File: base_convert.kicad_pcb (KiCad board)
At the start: 2 copper layers, 72 x 106 mm, 53 parts, among them SW1 SW_Push, SW10 SW_Push, SW11 SW_Push, SW12 SW_Push, SW13 SW_Push, SW14 SW_Push, SW15 SW_Push, SW16 SW_Push, SW17 SW_Push, SW18 SW_Push, SW19 SW_Push, SW2 SW_Push, SW20 SW_Push, SW21 SW_Push, SW22 SW_Push, SW23 SW_Push, SW24 SW_Push, SW25 SW_Push, SW26 SW_Push, SW27 SW_Push, SW28 SW_Push, SW29 SW_Push, SW3 SW_Push, SW30 SW_Push, SW31 SW_Push, SW32 SW_Push, SW4 SW_Push, SW5 SW_Push, SW6 SW_Push, SW7 SW_Push, SW8 SW_Push, SW9 SW_Push

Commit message: perlimanary prototype render
perlimanary prototype render complete
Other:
- board text added: "0"
- board text added: "1"
- board text added: "10"
- board text added: "11"
- board text added: "12"
- board text added: "13"
- board text added: "14"
- board text added: "15"
- board text added: "2"
- board text added: "3"
- board text added: "4"
- board text added: "5"
- board text added: "6"
- board text added: "7"
- board text added: "8"
- board text added: "9"
- board text added: "A"
- board text added: "B"
- board text added: "C"
- board text added: "D"
- board text added: "DEC"
- board text added: "E"
- board text added: "F"
- board text added: "HEX"

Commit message: update 7-segment display part number
Due to mismatch of display face using a mix of 4 digit and 1 digit displays does not look good. Swtiching all displays to be made up of 2 digit 7-segment display. Decimal display will have extra unused digit.
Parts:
- removed AFF1, AFF2, AFF3, AFF4, AFF5: DA04-11, Displays_7-Segment:DA04-11SURKWA
- added BT1: Battery, MPD:BC2AAPC, F.Cu at (195.2, 124.5)
- added C1: 10uF, Capacitors_SMD:C_0805, F.Cu at (335.6, 51.4)
- added C2: 100nF, Capacitors_SMD:C_0805, F.Cu at (340.1, 51.4)
- added DS1: LTD-4608JR, Lite-On:Display_Lite-On_LTD-4608JR, F.Cu at (189.6, 64.1)
- added DS2: LTD-4608JR, Lite-On:Display_Lite-On_LTD-4608JR, F.Cu at (96.0, 64.1)
- added DS3: LTD-4608JR, Lite-On:Display_Lite-On_LTD-4608JR, F.Cu at (121.3, 64.1)
- added DS4: LTD-4608JR, Lite-On:Display_Lite-On_LTD-4608JR, F.Cu at (176.8, 37.7)
- added DS5: LTD-4608JR, Lite-On:Display_Lite-On_LTD-4608JR, F.Cu at (152.8, 33.9)
- added J1: ISP, Pin_Headers:Pin_Header_Straight_1x04_Pitch2.54mm, F.Cu at (379.8, 21.2)
- added Q1: Q_PMOS_GSD, TO_SOT_Packages_SMD:SOT-23, F.Cu at (325.0, 52.4)
- added Q10: Q_PNP_BEC, TO_SOT_Packages_SMD:SOT-23, F.Cu at (269.3, 94.6)
- added Q11: Q_NPN_BEC, TO_SOT_Packages_SMD:SOT-23, F.Cu at (251.5, 100.0)
- added Q12: Q_NPN_BEC, TO_SOT_Packages_SMD:SOT-23, F.Cu at (252.7, 123.5)
- added Q13: Q_NPN_BEC, TO_SOT_Packages_SMD:SOT-23, F.Cu at (242.5, 107.1)
- added Q14: Q_NPN_BEC, TO_SOT_Packages_SMD:SOT-23, F.Cu at (224.6, 107.1)
- added Q15: Q_NPN_BEC, TO_SOT_Packages_SMD:SOT-23, F.Cu at (233.5, 107.1)
- added Q16: Q_NPN_BEC, TO_SOT_Packages_SMD:SOT-23, F.Cu at (217.4, 79.4)
- added Q17: Q_NPN_BEC, TO_SOT_Packages_SMD:SOT-23, F.Cu at (242.5, 100.0)
- added Q18: Q_PNP_BEC, TO_SOT_Packages_SMD:SOT-23, F.Cu at (353.3, 79.9)
- added Q19: Q_PNP_BEC, TO_SOT_Packages_SMD:SOT-23, F.Cu at (333.3, 96.8)
- added Q2: Q_PNP_BEC, TO_SOT_Packages_SMD:SOT-23, B.Cu at (181.7, 64.3)
- added Q20: Q_PNP_BEC, TO_SOT_Packages_SMD:SOT-23, F.Cu at (349.4, 86.9)
- added Q21: Q_PNP_BEC, TO_SOT_Packages_SMD:SOT-23, F.Cu at (340.5, 89.7)
- added Q22: Q_NPN_BEC, TO_SOT_Packages_SMD:SOT-23, F.Cu at (344.3, 72.8)
- added Q23: Q_NPN_BEC, TO_SOT_Packages_SMD:SOT-23, F.Cu at (344.3, 79.9)
- added Q24: Q_NPN_BEC, TO_SOT_Packages_SMD:SOT-23, F.Cu at (353.3, 72.8)
- added Q25: Q_NPN_BEC, TO_SOT_Packages_SMD:SOT-23, F.Cu at (324.4, 96.6)
- added Q26: Q_PNP_BEC, TO_SOT_Packages_SMD:SOT-23, F.Cu at (313.9, 20.7)
- added Q27: Q_NPN_BEC, TO_SOT_Packages_SMD:SOT-23, F.Cu at (313.9, 20.7)
- added Q3: Q_PNP_BEC, TO_SOT_Packages_SMD:SOT-23, F.Cu at (251.4, 107.1)
- added Q4: Q_PNP_BEC, TO_SOT_Packages_SMD:SOT-23, B.Cu at (234.4, 58.7)
- added Q5: Q_PNP_BEC, TO_SOT_Packages_SMD:SOT-23, B.Cu at (227.4, 60.2)
- added Q6: Q_PNP_BEC, TO_SOT_Packages_SMD:SOT-23, F.Cu at (237.3, 126.2)
- added Q7: Q_PNP_BEC, TO_SOT_Packages_SMD:SOT-23, F.Cu at (274.4, 87.5)
- added Q8: Q_PNP_BEC, TO_SOT_Packages_SMD:SOT-23, F.Cu at (257.7, 60.5)
- added Q9: Q_PNP_BEC, TO_SOT_Packages_SMD:SOT-23, F.Cu at (260.4, 107.1)
- added R1: 20k, Resistors_SMD:R_0805, F.Cu at (331.8, 51.6)
- added R10: 4.7k, Resistors_SMD:R_0805, F.Cu at (287.9, 84.5)
- added R11: 4.7k, Resistors_SMD:R_0805, F.Cu at (284.3, 86.1)
- added R12: 1k, Resistors_SMD:R_0603, B.Cu at (277.3, 99.0)
- added R13: 1k, Resistors_SMD:R_0603, B.Cu at (270.1, 106.0)
- added R14: 1k, Resistors_SMD:R_0603, B.Cu at (280.6, 96.8)
- added R15: 1k, Resistors_SMD:R_0603, B.Cu at (273.4, 106.0)
- added R16: 1k, Resistors_SMD:R_0603, B.Cu at (233.1, 73.4)
- added R17: 1k, Resistors_SMD:R_0603, B.Cu at (218.7, 71.7)
- added R18: 1k, Resistors_SMD:R_0603, B.Cu at (240.1, 72.4)
- added R19: 4.7k, Resistors_SMD:R_0805, F.Cu at (287.9, 89.9)
- added R2: 20k, Resistors_SMD:R_0805, F.Cu at (331.8, 57.1)
- added R20: 4.7k, Resistors_SMD:R_0805, F.Cu at (262.9, 93.7)
- added R21: 4.7k, Resistors_SMD:R_0805, F.Cu at (290.3, 79.0)
- added R22: 4.7k, Resistors_SMD:R_0805, F.Cu at (291.5, 84.5)
- added R23: 4.7k, Resistors_SMD:R_0805, F.Cu at (266.7, 100.8)
- added R24: 4.7k, Resistors_SMD:R_0805, F.Cu at (280.7, 86.1)
- added R25: 4.7k, Resistors_SMD:R_0805, F.Cu at (286.7, 79.0)
- added R26: 4.7k, Resistors_SMD:R_0805, F.Cu at (359.5, 84.5)
- added R27: 4.7k, Resistors_SMD:R_0805, F.Cu at (339.6, 101.4)
- added R28: 4.7k, Resistors_SMD:R_0805, F.Cu at (355.7, 86.1)
- added R29: 4.7k, Resistors_SMD:R_0805, F.Cu at (350.3, 93.1)
- added R3: 4.7k, Resistors_SMD:R_0805, B.Cu at (236.9, 64.2)
- added R30: 1k, Resistors_SMD:R_0603, F.Cu at (346.3, 98.4)
- added R31: 1k, Resistors_SMD:R_0603, F.Cu at (343.0, 95.7)
- added R32: 1k, Resistors_SMD:R_0603, F.Cu at (304.2, 101.7)
- added R33: 1k, Resistors_SMD:R_0603, F.Cu at (300.9, 101.7)
- added R34: 4.7k, Resistors_SMD:R_0805, F.Cu at (359.5, 79.0)
- added R35: 4.7k, Resistors_SMD:R_0805, F.Cu at (339.6, 95.9)
- added R36: 4.7k, Resistors_SMD:R_0805, F.Cu at (359.6, 72.0)
- added R37: 4.7k, Resistors_SMD:R_0805, F.Cu at (346.7, 93.1)
- added R38, R40: 4.7k, Resistors_SMD:R_0805, F.Cu at (313.9, 20.7)
- added R39: 1k, Resistors_SMD:R_0603, F.Cu at (313.9, 20.7)
- added R4: 4.7k, Resistors_SMD:R_0805, F.Cu at (266.6, 106.2)
- added R5: 4.7k, Resistors_SMD:R_0805, F.Cu at (270.3, 100.8)
- added R6: 4.7k, Resistors_SMD:R_0805, F.Cu at (280.7, 91.5)
- added R7: 4.7k, Resistors_SMD:R_0805, F.Cu at (284.3, 91.5)
- added R8: 4.7k, Resistors_SMD:R_0805, F.Cu at (273.9, 100.8)
- added R9: 4.7k, Resistors_SMD:R_0805, F.Cu at (293.9, 79.0)
- added SW33: B, Buttons_Switches_THT:SW_PUSH_6mm, F.Cu at (125.0, 137.5)
- added SW34: F, Buttons_Switches_THT:SW_PUSH_6mm, F.Cu at (125.0, 97.5)
- added U1: MSP430FR4133IPMR, Housings_QFP:LQFP-64_10x10mm_Pitch0.5mm, F.Cu at (102.5, 124.6)
- D1: value LED -> BIT3; footprint LEDs:LED_D3.0mm -> LEDs:LED_D5.0mm
- D10: value LED -> BIT5; footprint LEDs:LED_D3.0mm -> LEDs:LED_D5.0mm
- D11: value LED -> BIT9; footprint LEDs:LED_D3.0mm -> LEDs:LED_D5.0mm
- D12: value LED -> BIT13; footprint LEDs:LED_D3.0mm -> LEDs:LED_D5.0mm
- D13: value LED -> BIT0; footprint LEDs:LED_D3.0mm -> LEDs:LED_D5.0mm
- D14: value LED -> BIT4; footprint LEDs:LED_D3.0mm -> LEDs:LED_D5.0mm
- D15: value LED -> BIT8; footprint LEDs:LED_D3.0mm -> LEDs:LED_D5.0mm
- D16: value LED -> BIT12; footprint LEDs:LED_D3.0mm -> LEDs:LED_D5.0mm
- D2: value LED -> BIT7; footprint LEDs:LED_D3.0mm -> LEDs:LED_D5.0mm
- D3: value LED -> BIT11; footprint LEDs:LED_D3.0mm -> LEDs:LED_D5.0mm
- D4: value LED -> BIT15; footprint LEDs:LED_D3.0mm -> LEDs:LED_D5.0mm
- D5: value LED -> BIT2; footprint LEDs:LED_D3.0mm -> LEDs:LED_D5.0mm
- D6: value LED -> BIT6; footprint LEDs:LED_D3.0mm -> LEDs:LED_D5.0mm
- D7: value LED -> BIT10; footprint LEDs:LED_D3.0mm -> LEDs:LED_D5.0mm
- D8: value LED -> BIT14; footprint LEDs:LED_D3.0mm -> LEDs:LED_D5.0mm
- D9: value LED -> BIT1; footprint LEDs:LED_D3.0mm -> LEDs:LED_D5.0mm
- SW1: value SW_Push -> CLEAR; footprint Buttons_Switches_SMD:SW_SPST_FSMSM -> Buttons_Switches_THT:SW_PUSH_6mm
- SW10: value SW_Push -> B13; footprint Buttons_Switches_SMD:SW_SPST_FSMSM -> Buttons_Switches_THT:SW_PUSH_6mm
- SW11: value SW_Push -> B2; footprint Buttons_Switches_SMD:SW_SPST_FSMSM -> Buttons_Switches_THT:SW_PUSH_6mm
- SW12: value SW_Push -> B6; footprint Buttons_Switches_SMD:SW_SPST_FSMSM -> Buttons_Switches_THT:SW_PUSH_6mm
- SW13: value SW_Push -> B10; footprint Buttons_Switches_SMD:SW_SPST_FSMSM -> Buttons_Switches_THT:SW_PUSH_6mm
- SW14: value SW_Push -> B14; footprint Buttons_Switches_SMD:SW_SPST_FSMSM -> Buttons_Switches_THT:SW_PUSH_6mm
- SW15: value SW_Push -> B3; footprint Buttons_Switches_SMD:SW_SPST_FSMSM -> Buttons_Switches_THT:SW_PUSH_6mm
- SW16: value SW_Push -> B7; footprint Buttons_Switches_SMD:SW_SPST_FSMSM -> Buttons_Switches_THT:SW_PUSH_6mm
- SW17: value SW_Push -> B11; footprint Buttons_Switches_SMD:SW_SPST_FSMSM -> Buttons_Switches_THT:SW_PUSH_6mm
- SW18: value SW_Push -> B15; footprint Buttons_Switches_SMD:SW_SPST_FSMSM -> Buttons_Switches_THT:SW_PUSH_6mm
- SW19: value SW_Push -> 0; footprint Buttons_Switches_SMD:SW_SPST_FSMSM -> Buttons_Switches_THT:SW_PUSH_6mm
- SW2: value SW_Push -> SELECT; footprint Buttons_Switches_SMD:SW_SPST_FSMSM -> Switch_CK:DP4T_SS-24E06-TG5P
- SW20: value SW_Push -> 4; footprint Buttons_Switches_SMD:SW_SPST_FSMSM -> Buttons_Switches_THT:SW_PUSH_6mm
- SW21: value SW_Push -> 8; footprint Buttons_Switches_SMD:SW_SPST_FSMSM -> Buttons_Switches_THT:SW_PUSH_6mm
- SW22: value SW_Push -> C; footprint Buttons_Switches_SMD:SW_SPST_FSMSM -> Buttons_Switches_THT:SW_PUSH_6mm
- SW23: value SW_Push -> 1; footprint Buttons_Switches_SMD:SW_SPST_FSMSM -> Buttons_Switches_THT:SW_PUSH_6mm
- SW24: value SW_Push -> 5; footprint Buttons_Switches_SMD:SW_SPST_FSMSM -> Buttons_Switches_THT:SW_PUSH_6mm
- SW25: value SW_Push -> 9; footprint Buttons_Switches_SMD:SW_SPST_FSMSM -> Buttons_Switches_THT:SW_PUSH_6mm
- SW26: value SW_Push -> D; footprint Buttons_Switches_SMD:SW_SPST_FSMSM -> Buttons_Switches_THT:SW_PUSH_6mm
- SW27: value SW_Push -> 2; footprint Buttons_Switches_SMD:SW_SPST_FSMSM -> Buttons_Switches_THT:SW_PUSH_6mm
- SW28: value SW_Push -> 6; footprint Buttons_Switches_SMD:SW_SPST_FSMSM -> Buttons_Switches_THT:SW_PUSH_6mm
- SW29: value SW_Push -> A; footprint Buttons_Switches_SMD:SW_SPST_FSMSM -> Buttons_Switches_THT:SW_PUSH_6mm
- SW3: value SW_Push -> B0; footprint Buttons_Switches_SMD:SW_SPST_FSMSM -> Buttons_Switches_THT:SW_PUSH_6mm
- SW30: value SW_Push -> E; footprint Buttons_Switches_SMD:SW_SPST_FSMSM -> Buttons_Switches_THT:SW_PUSH_6mm
- SW31: value SW_Push -> 3; footprint Buttons_Switches_SMD:SW_SPST_FSMSM -> Buttons_Switches_THT:SW_PUSH_6mm
- SW32: value SW_Push -> 7; footprint Buttons_Switches_SMD:SW_SPST_FSMSM -> Buttons_Switches_THT:SW_PUSH_6mm
- SW4: value SW_Push -> B4; footprint Buttons_Switches_SMD:SW_SPST_FSMSM -> Buttons_Switches_THT:SW_PUSH_6mm
- SW5: value SW_Push -> B8; footprint Buttons_Switches_SMD:SW_SPST_FSMSM -> Buttons_Switches_THT:SW_PUSH_6mm
- SW6: value SW_Push -> B12; footprint Buttons_Switches_SMD:SW_SPST_FSMSM -> Buttons_Switches_THT:SW_PUSH_6mm
- SW7: value SW_Push -> B1; footprint Buttons_Switches_SMD:SW_SPST_FSMSM -> Buttons_Switches_THT:SW_PUSH_6mm
- SW8: value SW_Push -> B5; footprint Buttons_Switches_SMD:SW_SPST_FSMSM -> Buttons_Switches_THT:SW_PUSH_6mm
- SW9: value SW_Push -> B9; footprint Buttons_Switches_SMD:SW_SPST_FSMSM -> Buttons_Switches_THT:SW_PUSH_6mm
- moved D4 111.7 mm to (92.9, 78.9), turned to 0 degrees
- moved SW29 96.1 mm to (125.0, 147.5)
- moved SW1 92.1 mm to (167.0, 147.5), turned to 0 degrees
- moved D8 88.0 mm to (100.4, 78.9), turned to 0 degrees
- moved D3 86.6 mm to (122.9, 78.9), turned to 0 degrees
- moved SW30 83.0 mm to (125.0, 107.5)
- moved SW6 83.0 mm to (114.4, 91.7)
- moved SW18 79.9 mm to (91.9, 91.7), turned to 90 degrees
- moved SW27 76.0 mm to (153.0, 137.5)
- moved SW26 75.0 mm to (125.0, 117.5)
- moved SW10 74.1 mm to (106.9, 91.7)
- moved SW32 69.0 mm to (139.0, 117.5)
- moved SW23 68.4 mm to (139.0, 137.5)
- moved SW14 65.3 mm to (99.4, 91.7)
- moved D12 64.7 mm to (107.9, 78.9), turned to 0 degrees
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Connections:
- D1 pad 1: Net-(D1-Pad1) -> /Binary Display/BIT3
- D10 pad 1: Net-(D10-Pad1) -> /Binary Display/BIT1
- D11 pad 1: Net-(D11-Pad1) -> /Binary Display/BIT1
- D12 pad 1: Net-(D12-Pad1) -> /Binary Display/BIT1
- D13 pad 1: Net-(D13-Pad1) -> /Binary Display/BIT0
- D13 pad 2: Net-(D13-Pad2) -> Net-(D1-Pad2)
- D14 pad 1: Net-(D14-Pad1) -> /Binary Display/BIT0
- D14 pad 2: Net-(D14-Pad2) -> Net-(D10-Pad2)
- D15 pad 1: Net-(D15-Pad1) -> /Binary Display/BIT0
- D15 pad 2: Net-(D15-Pad2) -> Net-(D11-Pad2)
- D16 pad 1: Net-(D16-Pad1) -> /Binary Display/BIT0
- D16 pad 2: Net-(D16-Pad2) -> Net-(D12-Pad2)
- D2 pad 1: Net-(D2-Pad1) -> /Binary Display/BIT3
- D2 pad 2: Net-(D2-Pad2) -> Net-(D10-Pad2)
- D3 pad 1: Net-(D3-Pad1) -> /Binary Display/BIT3
- D3 pad 2: Net-(D3-Pad2) -> Net-(D11-Pad2)
- D4 pad 1: Net-(D4-Pad1) -> /Binary Display/BIT3
- D4 pad 2: Net-(D4-Pad2) -> Net-(D12-Pad2)
- D5 pad 1: Net-(D5-Pad1) -> /Binary Display/BIT2
- D5 pad 2: Net-(D5-Pad2) -> Net-(D1-Pad2)
- D6 pad 1: Net-(D6-Pad1) -> /Binary Display/BIT2
- D6 pad 2: Net-(D6-Pad2) -> Net-(D10-Pad2)
- D7 pad 1: Net-(D7-Pad1) -> /Binary Display/BIT2
- D7 pad 2: Net-(D7-Pad2) -> Net-(D11-Pad2)
- D8 pad 1: Net-(D8-Pad1) -> /Binary Display/BIT2
- D8 pad 2: Net-(D8-Pad2) -> Net-(D12-Pad2)
- D9 pad 1: Net-(D9-Pad1) -> /Binary Display/BIT1
- D9 pad 2: Net-(D9-Pad2) -> Net-(D1-Pad2)
- SW1 pad 1: Net-(SW1-Pad1) -> GND
- SW1 pad 2: Net-(SW1-Pad2) -> /CLEAR
- SW10 pad 1: Net-(SW10-Pad1) -> /BCOL1
- SW10 pad 2: Net-(SW10-Pad2) -> /BROW3
- SW11 pad 1: Net-(SW11-Pad1) -> /BCOL2
- SW11 pad 2: Net-(SW11-Pad2) -> /BROW0
- SW12 pad 1: Net-(SW12-Pad1) -> /BCOL2
- SW12 pad 2: Net-(SW12-Pad2) -> /BROW1
- SW13 pad 1: Net-(SW13-Pad1) -> /BCOL2
- SW13 pad 2: Net-(SW13-Pad2) -> /BROW2
- SW14 pad 1: Net-(SW14-Pad1) -> /BCOL2
- SW14 pad 2: Net-(SW14-Pad2) -> /BROW3
- SW15 pad 1: Net-(SW15-Pad1) -> /BCOL3
- SW15 pad 2: Net-(SW15-Pad2) -> /BROW0
- SW16 pad 1: Net-(SW16-Pad1) -> /BCOL3
- SW16 pad 2: Net-(SW16-Pad2) -> /BROW1
- SW17 pad 1: Net-(SW17-Pad1) -> /BCOL3
- SW17 pad 2: Net-(SW17-Pad2) -> /BROW2
- SW18 pad 1: Net-(SW18-Pad1) -> /BCOL3
- SW18 pad 2: Net-(SW18-Pad2) -> /BROW3
- SW19 pad 1: Net-(SW19-Pad1) -> /COL0
- SW19 pad 2: Net-(SW19-Pad2) -> /ROW0
- SW2 pad 1: Net-(SW2-Pad1) -> (no net)
- SW2 pad 2: Net-(SW2-Pad2) -> /DEC_INPUT
- SW20 pad 1: Net-(SW20-Pad1) -> /COL0
- SW20 pad 2: Net-(SW20-Pad2) -> /ROW1
- SW21 pad 1: Net-(SW21-Pad1) -> /COL0
- SW21 pad 2: Net-(SW21-Pad2) -> /ROW2
- SW22 pad 1: Net-(SW22-Pad1) -> /COL0
- SW22 pad 2: Net-(SW22-Pad2) -> /ROW3
- SW23 pad 1: Net-(SW23-Pad1) -> /COL1
- SW23 pad 2: Net-(SW23-Pad2) -> /ROW0
- SW24 pad 1: Net-(SW24-Pad1) -> /COL1
- SW24 pad 2: Net-(SW24-Pad2) -> /ROW1
- SW25 pad 1: Net-(SW25-Pad1) -> /COL1
- SW25 pad 2: Net-(SW25-Pad2) -> /ROW2
- SW26 pad 1: Net-(SW26-Pad1) -> /COL1
- SW26 pad 2: Net-(SW26-Pad2) -> /ROW3
- SW27 pad 1: Net-(SW27-Pad1) -> /COL2
- SW27 pad 2: Net-(SW27-Pad2) -> /ROW0
- SW28 pad 1: Net-(SW28-Pad1) -> /COL2
- SW28 pad 2: Net-(SW28-Pad2) -> /ROW1
- SW29 pad 1: Net-(SW29-Pad1) -> /COL2
- SW29 pad 2: Net-(SW29-Pad2) -> /ROW2
- SW3 pad 1: Net-(SW3-Pad1) -> /BCOL0
- SW3 pad 2: Net-(SW3-Pad2) -> /BROW0
- SW30 pad 1: Net-(SW30-Pad1) -> /COL2
- SW30 pad 2: Net-(SW30-Pad2) -> /ROW3
- SW31 pad 1: Net-(SW31-Pad1) -> /COL3
- SW31 pad 2: Net-(SW31-Pad2) -> /ROW0
- SW32 pad 1: Net-(SW32-Pad1) -> /COL3
- SW32 pad 2: Net-(SW32-Pad2) -> /ROW1
- SW4 pad 1: Net-(SW4-Pad1) -> /BCOL0
- SW4 pad 2: Net-(SW4-Pad2) -> /BROW1
- SW5 pad 1: Net-(SW5-Pad1) -> /BCOL0
- SW5 pad 2: Net-(SW5-Pad2) -> /BROW2
- SW6 pad 1: Net-(SW6-Pad1) -> /BCOL0
- SW6 pad 2: Net-(SW6-Pad2) -> /BROW3
- SW7 pad 1: Net-(SW7-Pad1) -> /BCOL1
- SW7 pad 2: Net-(SW7-Pad2) -> /BROW0
- SW8 pad 1: Net-(SW8-Pad1) -> /BCOL1
- SW8 pad 2: Net-(SW8-Pad2) -> /BROW1
- SW9 pad 1: Net-(SW9-Pad1) -> /BCOL1
- SW9 pad 2: Net-(SW9-Pad2) -> /BROW2
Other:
- board outline removed
- board text removed: "0"
- board text removed: "1"
- board text removed: "10"
- board text removed: "11"
- board text removed: "12"
- board text removed: "13"
- board text removed: "14"
- board text removed: "15"
- board text removed: "2"
- board text removed: "3"
- board text removed: "4"
- board text removed: "5"
- board text removed: "6"
- board text removed: "7"
- board text removed: "8"
- board text removed: "9"
- board text removed: "A"
- board text removed: "B"
- board text removed: "C"
- board text removed: "D"
- board text removed: "DEC"
- board text removed: "E"
- board text removed: "F"
- board text removed: "HEX"

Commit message: Push and shove for the win!
To Do: clean up.
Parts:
- BT1: value Battery -> 2x AA Battery
- Q2, Q4, Q5, R12, R13, R14, R15, R16, R17, R18, R3: moved to F.Cu
- SW1, SW10, SW11, SW12, SW13, SW14, SW15, SW16, SW17, SW18, SW19, SW20, SW21, SW22, SW23, SW24, SW25, SW26, SW27, SW28, SW29, SW3, SW30, SW31, SW32, SW33, SW34, SW4, SW5, SW6, SW7, SW8, SW9: footprint Buttons_Switches_THT:SW_PUSH_6mm -> Buttons_Switches_THT:SW_TH_Tactile_Omron_B3F-10xx
- moved J1 297.5 mm to (109.5, 145.5)
- moved R36 266.8 mm to (100.8, 136.9), turned to 180 degrees
- moved R34 266.8 mm to (100.8, 144.1), turned to 180 degrees
- moved Q24 263.9 mm to (97.1, 135.9), turned to 180 degrees
- moved Q22 257.0 mm to (97.1, 143.2), turned to 180 degrees
- moved R30 256.5 mm to (93.8, 143.2)
- moved Q23 254.3 mm to (97.1, 139.6), turned to 180 degrees
- moved R31 253.1 mm to (93.8, 139.6)
- moved R37 249.2 mm to (100.8, 133.3), turned to 180 degrees
- moved C2 245.5 mm to (110.7, 138.8), turned to 180 degrees
- moved R1 243.9 mm to (105.5, 142.7), turned to 90 degrees
- moved R35 243.0 mm to (100.8, 140.5), turned to 180 degrees
- moved C1 242.1 mm to (110.7, 141.0), turned to 180 degrees
- moved R2 239.6 mm to (106.5, 138.8)
- moved R39 235.2 mm to (93.8, 103.5), turned to 180 degrees
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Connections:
- net /LED_BIT0 renamed /Binary Display/LED_BIT0
- net /LED_BIT1 renamed /Binary Display/LED_BIT1
- net /LED_BIT2 renamed /Binary Display/LED_BIT2
- net /LED_BIT3 renamed /Binary Display/LED_BIT3
- net /NIBBLE0 renamed /Binary Display/NIBBLE0
- net /NIBBLE1 renamed /Binary Display/NIBBLE1
- net /NIBBLE2 renamed /Binary Display/NIBBLE2
- net /NIBBLE3 renamed /Binary Display/NIBBLE3
- net /SEG_A renamed /7 Segment Displays/SEG-A
- net /SEG_B renamed /7 Segment Displays/SEG-B
- net /SEG_C renamed /7 Segment Displays/SEG-C
- net /SEG_D renamed /7 Segment Displays/SEG-D
- net /SEG_DP renamed /7 Segment Displays/SEG-DP
- net /SEG_E renamed /7 Segment Displays/SEG-E
- net /SEG_F renamed /7 Segment Displays/SEG-F
- net /SEG_G renamed /7 Segment Displays/SEG-G
- DS1 pad 4: /HEX2 -> /7 Segment Displays/HEX2
- DS1 pad 9: /HEX1 -> /7 Segment Displays/HEX1
- DS2 pad 4: /HEX4 -> /7 Segment Displays/HEX4
- DS2 pad 9: /HEX3 -> /7 Segment Displays/HEX3
- DS3 pad 4: /DEC2 -> /7 Segment Displays/DEC2
- DS3 pad 9: /DEC1 -> /7 Segment Displays/DEC1
- DS4 pad 4: /DEC4 -> /7 Segment Displays/DEC4
- DS4 pad 9: /DEC3 -> /7 Segment Displays/DEC3
- DS5 pad 4: /DEC6 -> /7 Segment Displays/DEC6
- DS5 pad 9: /DEC5 -> /7 Segment Displays/DEC5
- Q1 pad 2: VCC -> Net-(Q1-Pad2)
- Q1 pad 3: Net-(Q1-Pad3) -> Net-(BT1-Pad1)
- Q10 pad 2: /DEC5 -> /7 Segment Displays/DEC5
- Q2 pad 2: /HEX1 -> /7 Segment Displays/HEX1
- Q26 pad 2: /DEC6 -> /7 Segment Displays/DEC6
- Q3 pad 2: /HEX2 -> /7 Segment Displays/HEX2
- Q4 pad 2: /HEX3 -> /7 Segment Displays/HEX3
- Q5 pad 2: /HEX4 -> /7 Segment Displays/HEX4
- Q6 pad 2: /DEC1 -> /7 Segment Displays/DEC1
- Q7 pad 2: /DEC2 -> /7 Segment Displays/DEC2
- Q8 pad 2: /DEC3 -> /7 Segment Displays/DEC3
- Q9 pad 2: /DEC4 -> /7 Segment Displays/DEC4
- R10 pad 2: /DEC4 -> /7 Segment Displays/~DEC4
- R11 pad 2: /DEC5 -> /7 Segment Displays/~DEC5
- R3 pad 2: /HEX1 -> /7 Segment Displays/~HEX1
- R38 pad 2: /DEC6 -> /7 Segment Displays/~DEC6
- R4 pad 2: /HEX2 -> /7 Segment Displays/~HEX2
- R5 pad 2: /HEX3 -> /7 Segment Displays/~HEX3
- R6 pad 2: /HEX4 -> /7 Segment Displays/~HEX4
- R7 pad 2: /DEC1 -> /7 Segment Displays/~DEC1
- R8 pad 2: /DEC2 -> /7 Segment Displays/~DEC2
- R9 pad 2: /DEC3 -> /7 Segment Displays/~DEC3
- SW1 pad 2: /CLEAR -> (no net)
- SW10 pad 2: /BROW3 -> Net-(SW10-Pad2)
- SW11 pad 1: /BCOL2 -> (no net)
- SW11 pad 2: /BROW0 -> Net-(SW11-Pad2)
- SW12 pad 1: /BCOL2 -> (no net)
- SW12 pad 2: /BROW1 -> Net-(SW11-Pad2)
- SW13 pad 1: /BCOL2 -> (no net)
- SW13 pad 2: /BROW2 -> Net-(SW11-Pad2)
- SW14 pad 2: /BROW3 -> Net-(SW11-Pad2)
- SW15 pad 1: /BCOL3 -> (no net)
- SW15 pad 2: /BROW0 -> Net-(SW15-Pad2)
- SW16 pad 1: /BCOL3 -> (no net)
- SW16 pad 2: /BROW1 -> Net-(SW15-Pad2)
- SW17 pad 1: /BCOL3 -> (no net)
- SW17 pad 2: /BROW2 -> Net-(SW15-Pad2)
- SW18 pad 2: /BROW3 -> Net-(SW15-Pad2)
- SW19 pad 1: /COL0 -> /COL1
- SW19 pad 2: /ROW0 -> (no net)
- SW2 pad 10: Net-(BT1-Pad1) -> Net-(Q1-Pad2)
- SW2 pad 11: Net-(Q1-Pad3) -> VCC
- SW2 pad 7: Net-(Q1-Pad3) -> VCC
- SW2 pad 8: Net-(Q1-Pad3) -> VCC
- SW20 pad 1: /COL0 -> /COL2
- SW20 pad 2: /ROW1 -> (no net)
- SW21 pad 1: /COL0 -> /COL1
- SW21 pad 2: /ROW2 -> (no net)
- SW22 pad 1: /COL0 -> /COL3
- SW22 pad 2: /ROW3 -> (no net)
- SW23 pad 1: /COL1 -> /COL2
- SW23 pad 2: /ROW0 -> (no net)
- SW24 pad 2: /ROW1 -> (no net)
- SW25 pad 1: /COL1 -> /COL0
- SW25 pad 2: /ROW2 -> (no net)
- SW26 pad 1: /COL1 -> /COL3
- SW26 pad 2: /ROW3 -> (no net)
- SW27 pad 1: /COL2 -> /COL1
- SW27 pad 2: /ROW0 -> (no net)
- SW28 pad 1: /COL2 -> /COL0
- SW28 pad 2: /ROW1 -> (no net)
- SW29 pad 2: /ROW2 -> (no net)
- SW3 pad 1: /BCOL0 -> (no net)
- SW3 pad 2: /BROW0 -> Net-(SW3-Pad2)
- SW30 pad 1: /COL2 -> /COL3
- SW30 pad 2: /ROW3 -> (no net)
- SW31 pad 1: /COL3 -> /COL0
- SW31 pad 2: /ROW0 -> (no net)
- SW32 pad 1: /COL3 -> /COL2
- SW32 pad 2: /ROW1 -> (no net)
- SW33 pad 2: /ROW2 -> (no net)
- SW34 pad 1: /COL3 -> /COL0
- SW34 pad 2: /ROW3 -> (no net)
- SW4 pad 1: /BCOL0 -> (no net)
- SW4 pad 2: /BROW1 -> Net-(SW3-Pad2)
- SW5 pad 1: /BCOL0 -> (no net)
- SW5 pad 2: /BROW2 -> Net-(SW3-Pad2)
- SW6 pad 2: /BROW3 -> Net-(SW3-Pad2)
- SW7 pad 1: /BCOL1 -> (no net)
- SW7 pad 2: /BROW0 -> Net-(SW10-Pad2)
- SW8 pad 1: /BCOL1 -> (no net)
- SW8 pad 2: /BROW1 -> Net-(SW10-Pad2)
- SW9 pad 1: /BCOL1 -> (no net)
- SW9 pad 2: /BROW2 -> Net-(SW10-Pad2)
- U1 pad 1: /DEC_INPUT -> (no net)
- U1 pad 16: (no net) -> /CLEAR
- U1 pad 2: /HEX_INPUT -> (no net)
- U1 pad 3: /BIN_INPUT -> (no net)
- U1 pad 33: (no net) -> /BIN_INPUT
- U1 pad 34: (no net) -> /HEX_INPUT
- U1 pad 35: (no net) -> /DEC_INPUT
- U1 pad 39: /DEC6 -> /7 Segment Displays/~DEC6
- U1 pad 4: /CLEAR -> (no net)
- U1 pad 40: /DEC5 -> /7 Segment Displays/~DEC5
- U1 pad 41: /DEC4 -> /7 Segment Displays/~DEC4
- U1 pad 42: /DEC3 -> /7 Segment Displays/~DEC3
- U1 pad 43: /DEC2 -> /7 Segment Displays/~DEC2
- U1 pad 44: /DEC1 -> /7 Segment Displays/~DEC1
- U1 pad 45: /HEX4 -> /7 Segment Displays/~HEX4
- U1 pad 46: /HEX3 -> /7 Segment Displays/~HEX3
- U1 pad 47: /HEX2 -> /7 Segment Displays/~HEX2
- U1 pad 48: /HEX1 -> /7 Segment Displays/~HEX1
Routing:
- net VCC: track 0.00 -> 232.9 mm
- net /7 Segment Displays/B: track 0.00 -> 183.4 mm, vias 0 -> 1
- net /Binary Display/BIT1: track 0.00 -> 179.3 mm, vias 0 -> 1
- net /7 Segment Displays/A: track 0.00 -> 178.1 mm
- net /Binary Display/BIT0: track 0.00 -> 174.9 mm, vias 0 -> 1
- net /Binary Display/BIT2: track 0.00 -> 174.7 mm, vias 0 -> 1
- net /7 Segment Displays/F: track 0.00 -> 171.5 mm, vias 0 -> 2
- net /Binary Display/BIT3: track 0.00 -> 168.7 mm, vias 0 -> 3
- net /7 Segment Displays/D: track 0.00 -> 168.5 mm, vias 0 -> 2
- net /7 Segment Displays/G: track 0.00 -> 168.0 mm, vias 0 -> 3
- net /7 Segment Displays/C: track 0.00 -> 162.8 mm, vias 0 -> 1
- net /7 Segment Displays/E: track 0.00 -> 161.5 mm, vias 0 -> 2
- net /7 Segment Displays/DP: track 0.00 -> 142.7 mm, vias 0 -> 2
- net /BROW0: track 0.00 -> 135.3 mm
- net /COL0: track 0.00 -> 133.2 mm, vias 0 -> 1
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- added copper zone on B.Cu, net GND
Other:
- board outline added: 121 x 96 mm
- net class Default: via_dia 0.6 -> 0.7

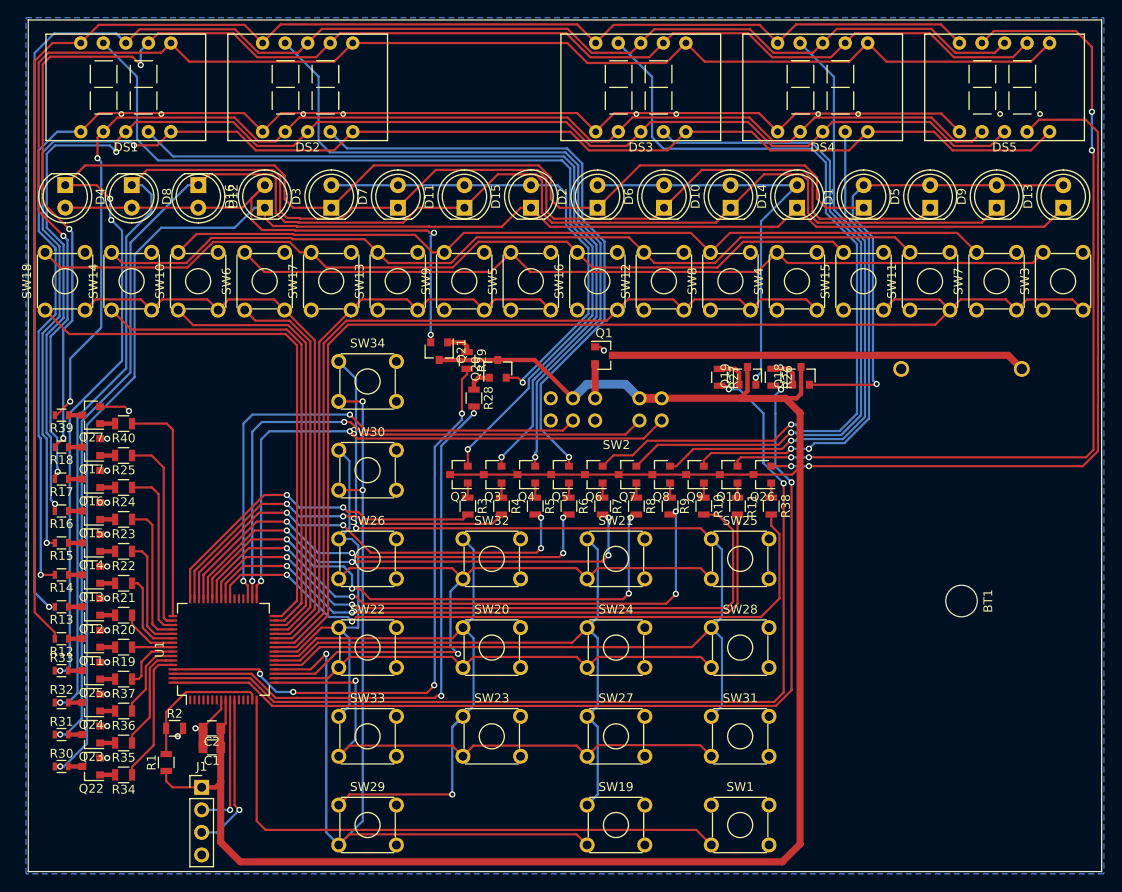
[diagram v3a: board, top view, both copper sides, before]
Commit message: add header to break out 3 unsused pins just in case
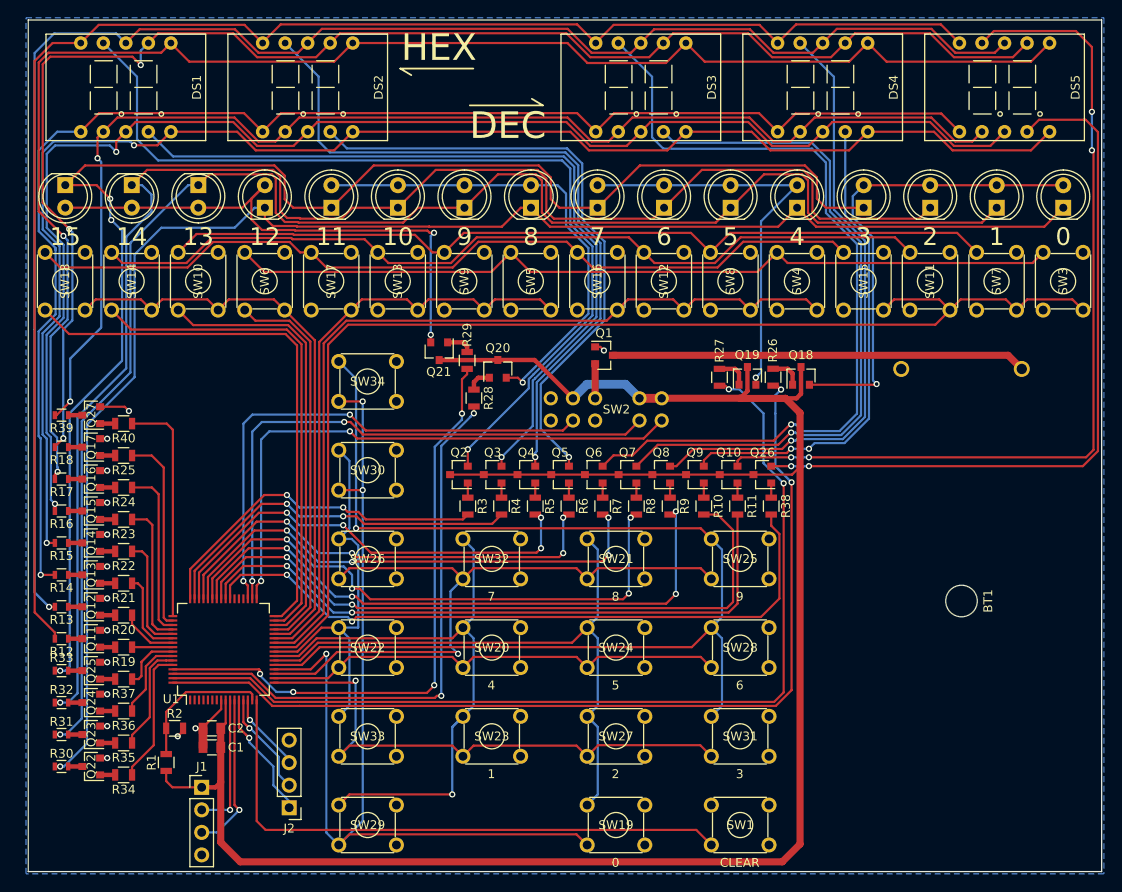
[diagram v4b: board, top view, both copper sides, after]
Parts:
- added J2: Extra, Pin_Headers:Pin_Header_Straight_1x04_Pitch2.54mm, F.Cu at (119.4, 147.8)
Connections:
- U1 pad 12: (no net) -> /P4_0
- U1 pad 13: (no net) -> /P8_3
- U1 pad 14: (no net) -> /P8_2
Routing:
- net /P4_0: track 0.00 -> 14.5 mm, vias 0 -> 1
- net /P8_3: track 0.00 -> 11.8 mm, vias 0 -> 1
- net /P8_2: track 0.00 -> 9.00 mm, vias 0 -> 1
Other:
- board text added: "0"
- board text added: "1"
- board text added: "10"
- board text added: "11"
- board text added: "12"
- board text added: "13"
- board text added: "14"
- board text added: "15"
- board text added: "2"
- board text added: "3"
- board text added: "4"
- board text added: "5"
- board text added: "6"
- board text added: "7"
- board text added: "8"
- board text added: "9"
- board text added: "DEC"
- board text added: "HEX"

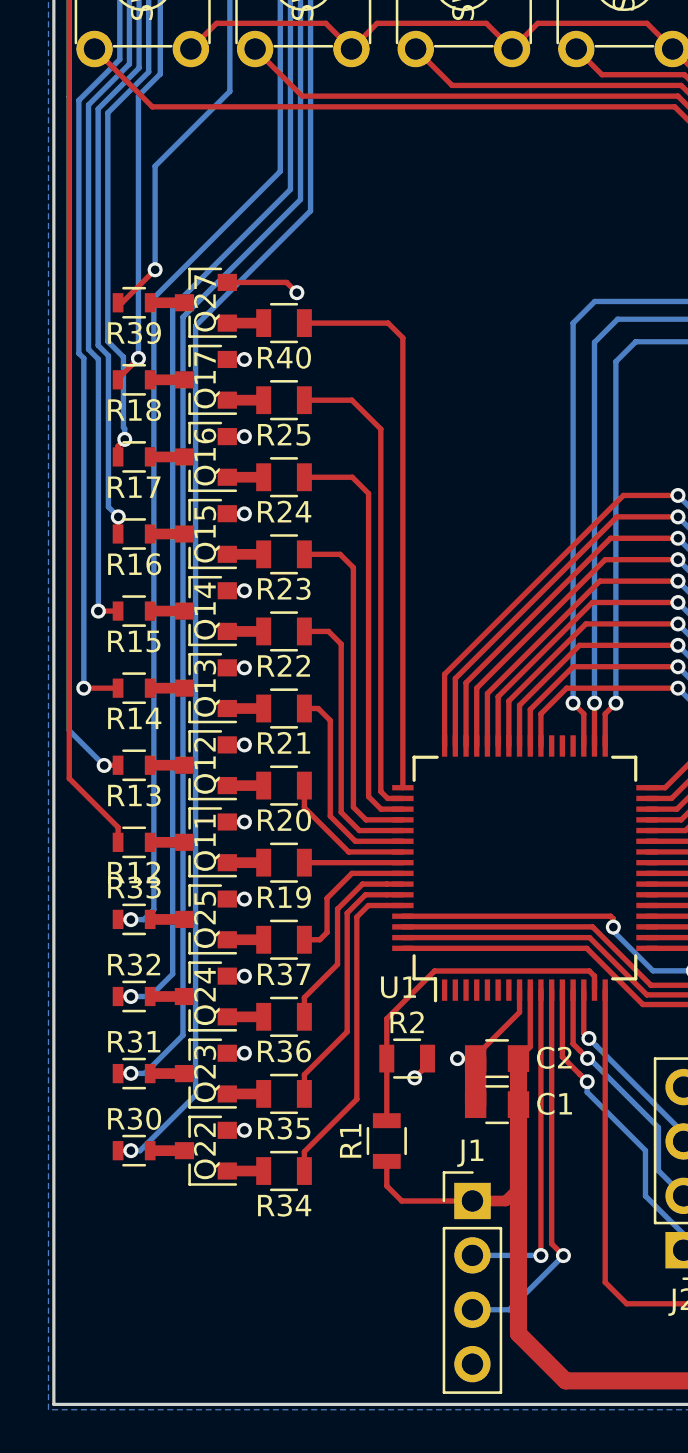
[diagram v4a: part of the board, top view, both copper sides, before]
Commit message: Silkscreen cleanup, add 3d models for render
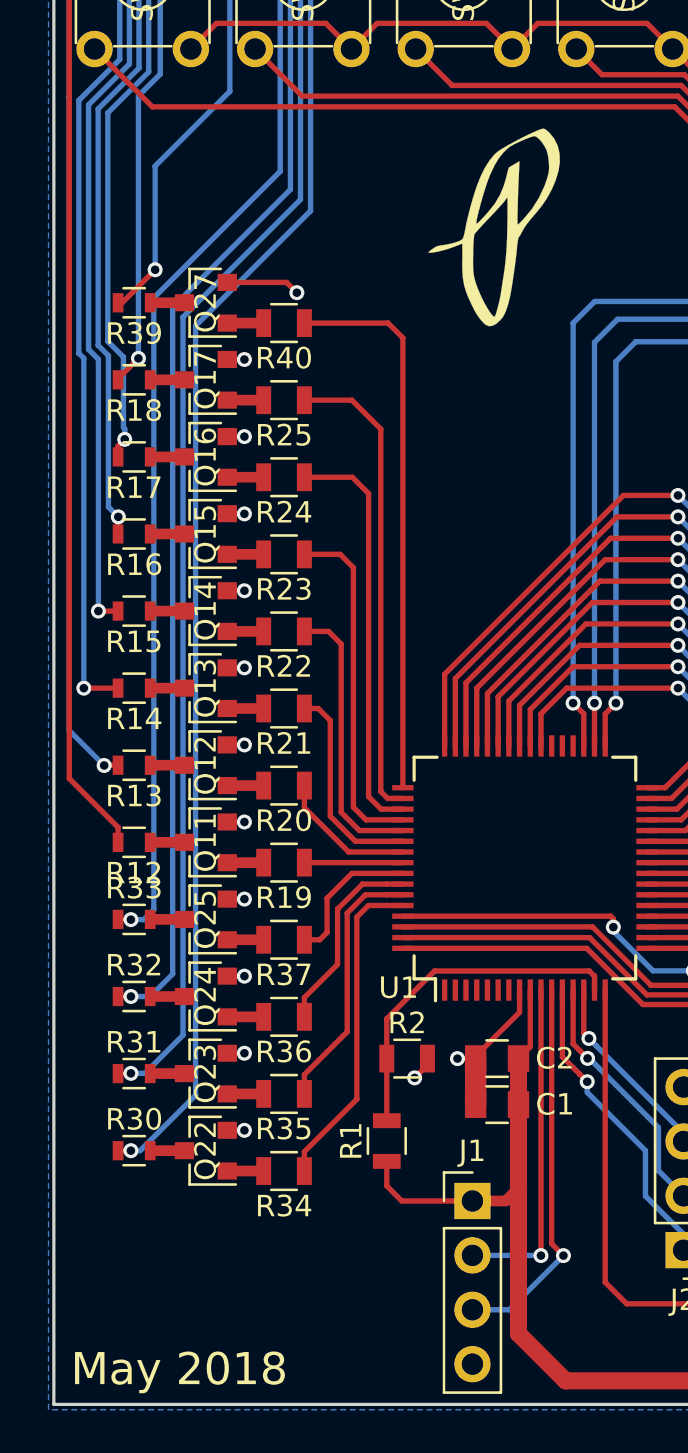
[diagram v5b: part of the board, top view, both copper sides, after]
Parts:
- added G***: LOGO, Artwork:logo_9x6mm, F.Cu at (110.5, 100.0)
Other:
- board text added: "May 2018"
